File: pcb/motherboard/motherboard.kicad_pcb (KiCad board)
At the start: 2 copper layers, 64 parts, among them J1 BOOT PIN HEADER, J2 ST-Link, J3 UART_USB, J4 I2C_HEADER, SW1 STM_RST, SW2 GEN_MAZE, SW3 TOGGLE_MAZE, SW4 SOLVE_MAZE, U1 STM32F103C8Tx, U2 CH340C, U3 TPS5420D, U4 TPS5420D, U5 AMS1117-3.3, U6 PCA9306D, Y1 8MHz, Y2 32.768KHz

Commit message: placed general position of motherboard pcb components
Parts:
- added J10: M20-7820646, KiCad:HDRV6W70P0X254_1X6_1564X250X850P, F.Cu at (246.6, 51.6)
- added J11: M20-7820646, KiCad:HDRV6W70P0X254_1X6_1564X250X850P, F.Cu at (246.6, 55.7)
- added J12: M20-7820646, KiCad:HDRV6W70P0X254_1X6_1564X250X850P, F.Cu at (246.6, 59.7)
- added J13: M20-7820646, KiCad:HDRV6W70P0X254_1X6_1564X250X850P, F.Cu at (246.6, 63.8)
- added J14: M20-7820646, KiCad:HDRV6W70P0X254_1X6_1564X250X850P, F.Cu at (246.6, 67.8)
- added J15: M20-7820646, KiCad:HDRV6W70P0X254_1X6_1564X250X850P, F.Cu at (246.6, 71.9)
- added J16: M20-7820646, KiCad:HDRV6W70P0X254_1X6_1564X250X850P, F.Cu at (246.6, 75.9)
- added J5: KPJX-4S-S, KiCad1:KPJX4SS, F.Cu at (69.2, 20.5)
- added J6: SPI_TEST, Connector_PinHeader_2.54mm:PinHeader_1x05_P2.54mm_Vertical, F.Cu at (237.2, 106.7)
- added J7: M20-7820646, KiCad:HDRV6W70P0X254_1X6_1564X250X850P, F.Cu at (246.6, 39.5)
- added J8: M20-7820646, KiCad:HDRV6W70P0X254_1X6_1564X250X850P, F.Cu at (246.6, 43.5)
- added J9: M20-7820646, KiCad:HDRV6W70P0X254_1X6_1564X250X850P, F.Cu at (246.6, 47.6)
- added TP1: GND, TestPoint:TestPoint_Pad_2.0x2.0mm, F.Cu at (237.0, 90.2)
- added TP2: 3V3, TestPoint:TestPoint_Pad_2.0x2.0mm, F.Cu at (237.0, 94.3)
- added TP3: 5V, TestPoint:TestPoint_Pad_2.0x2.0mm, F.Cu at (237.0, 98.3)
- added TP4: 5V5, TestPoint:TestPoint_Pad_2.0x2.0mm, F.Cu at (237.0, 102.4)
- added TP5: UART_RX, TestPoint:TestPoint_Pad_2.0x2.0mm, F.Cu at (241.0, 90.2)
- added TP6: UART_TX, TestPoint:TestPoint_Pad_2.0x2.0mm, F.Cu at (241.0, 94.3)
- added TP7: 12V, TestPoint:TestPoint_Pad_2.0x2.0mm, F.Cu at (241.0, 98.3)
- added U7: 74HC138, Package_SO:SOIC-16_3.9x9.9mm_P1.27mm, F.Cu at (184.9, 49.3)
- moved SW1 155.7 mm to (37.6, 93.2)
- moved R2 143.4 mm to (42.2, 96.0), turned to 180 degrees
- moved C5 142.2 mm to (42.2, 93.2), turned to 180 degrees
- moved Y2 138.0 mm to (51.3, 99.1), turned to 90 degrees
- moved Y1 137.6 mm to (51.3, 103.6), turned to 90 degrees
- moved C10 128.8 mm to (56.4, 94.5), turned to 180 degrees
- moved C7 128.2 mm to (56.4, 93.0), turned to 180 degrees
- moved C9 127.9 mm to (56.4, 109.2)
- moved C8 117.8 mm to (66.5, 109.2)
- moved U2 116.9 mm to (51.8, 138.2)
- moved R12 116.4 mm to (69.7, 65.7)
- moved R11 116.4 mm to (69.6, 63.8)
- moved C15 116.1 mm to (42.0, 133.4)
- moved C16 115.1 mm to (74.5, 40.5)
- moved C6 113.2 mm to (71.1, 98.6)
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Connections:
- U1 pad 13: /STM32/PA4 -> /SPI_CS
- U1 pad 14: /STM32/PA5 -> /SPI_CLK
- U1 pad 15: /STM32/PA6 -> /SPI_MISO
- U1 pad 16: /STM32/PA7 -> /SPI_MOSI
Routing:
- net Net-(U3-VSNS): vias 0 -> 2
- net Net-(D2-K): vias 0 -> 2
- net Net-(D1-K): vias 0 -> 2
- net GND: vias 0 -> 19
- net /USB_D-: vias 0 -> 2
- net /USB_D+: vias 0 -> 2
- net /UART_TX: vias 0 -> 2
- net /UART_RX: vias 0 -> 2
- net /TG_MAZE: vias 0 -> 1
- net /STM32/RST: vias 0 -> 1
- net /STM32/PB7: vias 0 -> 2
- net /STM32/PB6: vias 0 -> 2
- net /STM32/PB5: vias 0 -> 2
- net /STM32/PB11: vias 0 -> 2
- net /STM32/PB10: vias 0 -> 5
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
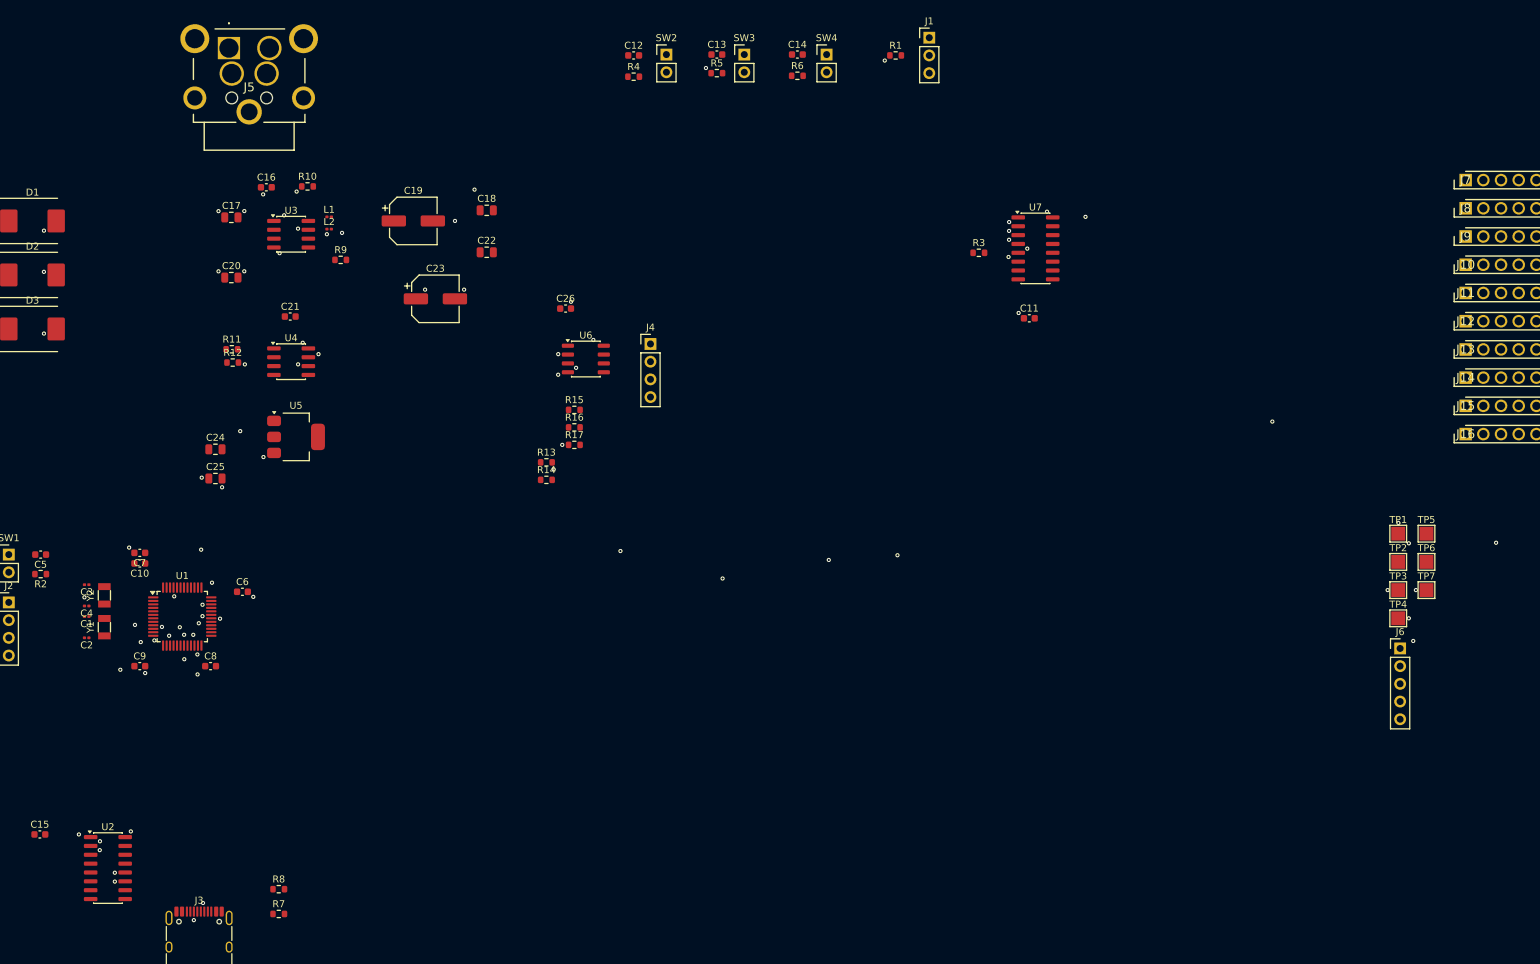
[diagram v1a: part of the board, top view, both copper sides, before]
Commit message: consolidated BOM for motherboard, added terminal blocks for external motors
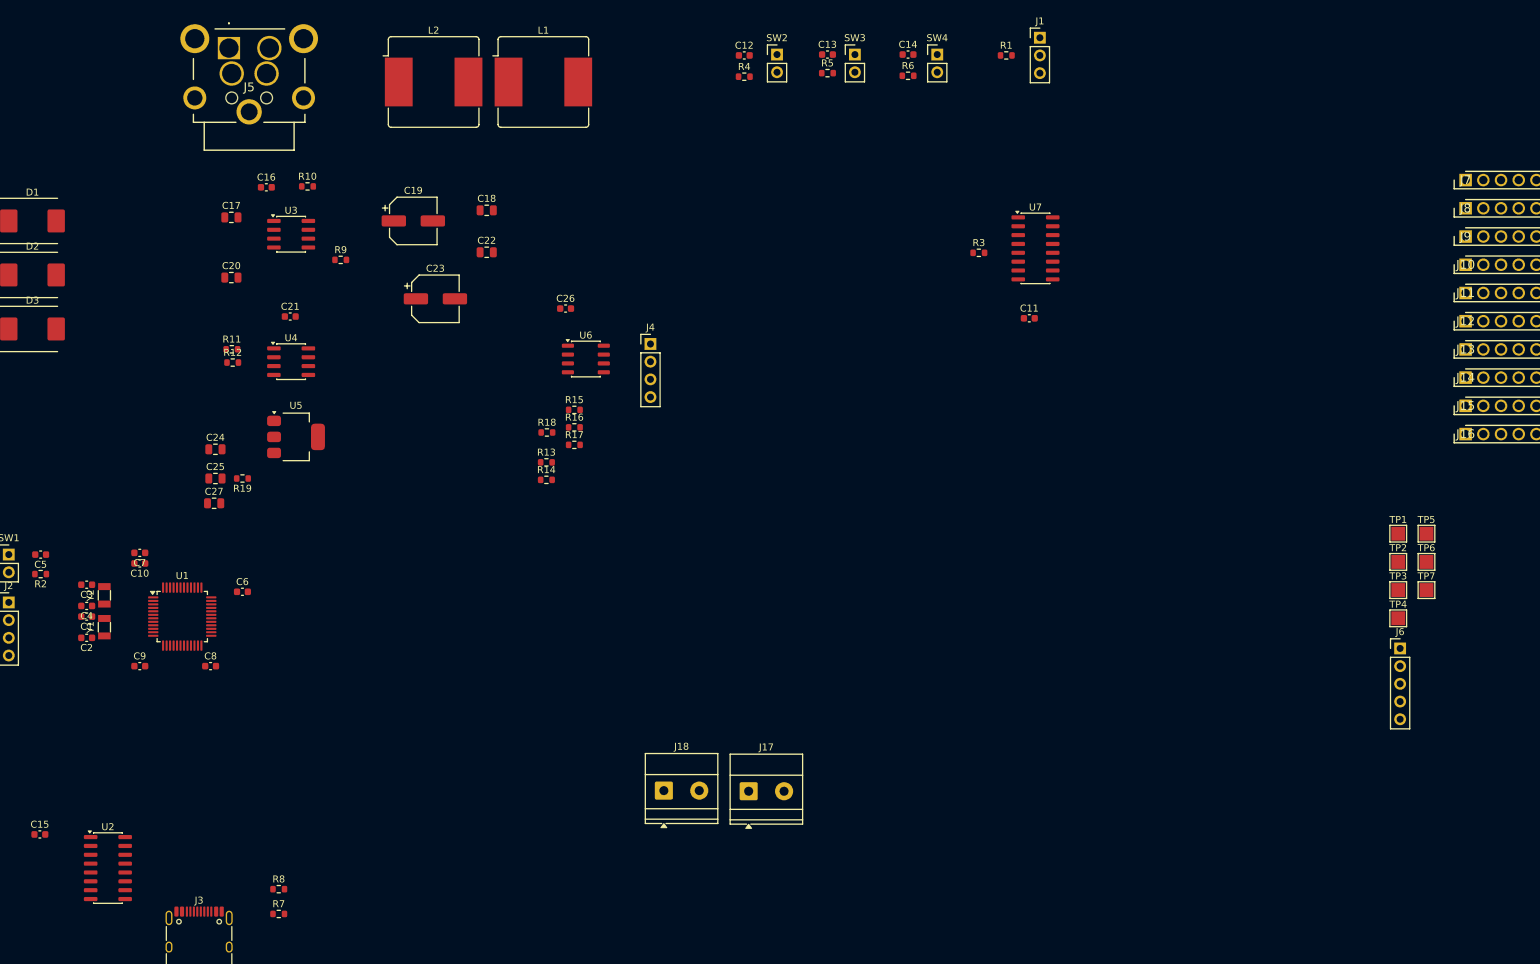
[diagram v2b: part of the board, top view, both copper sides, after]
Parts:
- added C27: 10uF, Capacitor_SMD:C_0805_2012Metric, F.Cu at (67.1, 85.9)
- added J17: Terminal 1, TerminalBlock_Phoenix:TerminalBlock_Phoenix_MKDS-1,5-2-5.08_1x02_P5.08mm_Horizontal, F.Cu at (143.8, 127.2)
- added J18: Terminal 2, TerminalBlock_Phoenix:TerminalBlock_Phoenix_MKDS-1,5-2-5.08_1x02_P5.08mm_Horizontal, F.Cu at (131.6, 127.1)
- added R18: 100k, Resistor_SMD:R_0603_1608Metric, F.Cu at (114.8, 75.7)
- added R19: 0.5, Resistor_SMD:R_0603_1608Metric, F.Cu at (71.1, 82.3)
- C1, C2, C3, C4: footprint Capacitor_SMD:C_0201_0603Metric -> Capacitor_SMD:C_0603_1608Metric
- C25: value 22uF -> 10uF
- L1, L2: footprint Inductor_SMD:L_0201_0603Metric -> Inductor_SMD:L_Bourns_SRR1208_12.7x12.7mm
- R13, R14, R15, R16: value 4.7k -> 5.1k
- R17: value 200k -> 100k
- moved L1 36.3 mm to (114.3, 25.4)
- moved L2 25.9 mm to (98.6, 25.4)
- moved C13 15.9 mm to (155.1, 21.5)
- moved C14 15.9 mm to (166.6, 21.5)
- moved J1 15.9 mm to (185.5, 19.1)
- moved R1 15.9 mm to (180.7, 21.6)
- moved R5 15.9 mm to (155.1, 24.1)
- moved R6 15.9 mm to (166.6, 24.5)
- moved SW2 15.9 mm to (147.8, 21.5)
- moved SW3 15.9 mm to (159.0, 21.5)
- moved SW4 15.9 mm to (170.8, 21.5)
- moved C12 15.9 mm to (143.1, 21.6)
- moved R4 15.9 mm to (143.1, 24.6)
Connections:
- C25 pad 2: GND -> Net-(C25-Pad2)
- R17 pad 1: +5V -> Net-(R17-Pad1)
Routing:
- net Net-(U3-VSNS): vias 2 -> 0
- net Net-(D2-K): vias 2 -> 0
- net Net-(D1-K): vias 2 -> 0
- net GND: vias 19 -> 0
- net /USB_D-: vias 2 -> 0
- net /USB_D+: vias 2 -> 0
- net /UART_TX: vias 2 -> 0
- net /UART_RX: vias 2 -> 0
- net /TG_MAZE: vias 1 -> 0
- net /STM32/RST: vias 1 -> 0
- net /STM32/PB7: vias 2 -> 0
- net /STM32/PB6: vias 2 -> 0
- net /STM32/PB5: vias 2 -> 0
- net /STM32/PB11: vias 2 -> 0
- net /STM32/PB10: vias 5 -> 0
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
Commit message: added 3d models for remaining components
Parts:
- added H1: MountingHole, MountingHole:MountingHole_4.3mm_M4, F.Cu at (162.6, 154.9)
- added H2: MountingHole, MountingHole:MountingHole_4.3mm_M4, F.Cu at (162.6, 165.1)
- added H3: MountingHole, MountingHole:MountingHole_4.3mm_M4, F.Cu at (162.6, 175.2)
- added H4: MountingHole, MountingHole:MountingHole_4.3mm_M4, F.Cu at (162.6, 185.4)
- moved J18 144.5 mm to (29.5, 24.8)
- moved J17 144.5 mm to (41.7, 24.9)
- moved J6 46.1 mm to (275.3, 132.6)
- moved TP5 46.1 mm to (279.1, 116.1)
- moved TP6 46.1 mm to (279.1, 120.2)
- moved TP7 46.1 mm to (279.1, 124.2)
- moved TP1 46.1 mm to (275.1, 116.1)
- moved TP2 46.1 mm to (275.1, 120.2)
- moved TP3 46.1 mm to (275.1, 124.2)
- moved TP4 46.1 mm to (275.1, 128.3)
- moved C11 29.7 mm to (156.1, 49.1)
- moved R3 29.7 mm to (148.8, 39.8)
- moved U7 29.7 mm to (157.0, 39.1)
- moved J16 27.5 mm to (265.9, 56.4)
- moved J10 27.5 mm to (265.9, 32.1)
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
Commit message: finished initial PCB layout for motherboard
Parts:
- removed H2: MountingHole, MountingHole:MountingHole_4.3mm_M4
- removed J10, J12, J14, J16, J8: M20-7820646, KiCad:HDRV6W70P0X254_1X6_1564X250X850P
- added C28: 220uF, Capacitor_SMD:CP_Elec_6.3x5.4, F.Cu at (180.0, 49.4)
- added C29: 220uF, Capacitor_SMD:CP_Elec_6.3x5.4, F.Cu at (149.8, 49.4)
- added C30: 220uF, Capacitor_SMD:CP_Elec_6.3x5.4, F.Cu at (157.4, 49.4)
- added C31: 220uF, Capacitor_SMD:CP_Elec_6.3x5.4, F.Cu at (164.9, 49.4)
- added C32: 220uF, Capacitor_SMD:CP_Elec_6.3x5.4, F.Cu at (172.4, 49.4)
- added J19: Terminal Block, TerminalBlock_Phoenix:TerminalBlock_Phoenix_MKDS-1,5-3-5.08_1x03_P5.08mm_Horizontal, F.Cu at (198.5, 57.0)
- added J20: Terminal Block, TerminalBlock_Phoenix:TerminalBlock_Phoenix_MKDS-1,5-3-5.08_1x03_P5.08mm_Horizontal, F.Cu at (198.5, 73.2)
- added J21: Terminal Block, TerminalBlock_Phoenix:TerminalBlock_Phoenix_MKDS-1,5-3-5.08_1x03_P5.08mm_Horizontal, F.Cu at (198.5, 89.5)
- added J22: Terminal Block, TerminalBlock_Phoenix:TerminalBlock_Phoenix_MKDS-1,5-3-5.08_1x03_P5.08mm_Horizontal, F.Cu at (198.5, 105.8)
- added J23: Terminal Block, TerminalBlock_Phoenix:TerminalBlock_Phoenix_MKDS-1,5-3-5.08_1x03_P5.08mm_Horizontal, F.Cu at (198.5, 122.0)
- added TP8: GND, TestPoint:TestPoint_Pad_2.0x2.0mm, F.Cu at (157.7, 125.6)
- moved J6 169.3 mm to (116.0, 75.3)
- moved TP4 169.1 mm to (127.7, 45.3)
- moved TP1 168.5 mm to (122.1, 45.3)
- moved TP2 167.9 mm to (122.1, 50.9)
- moved TP3 164.6 mm to (127.7, 50.9)
- moved J18 161.6 mm to (146.4, 136.3)
- moved J17 161.6 mm to (158.6, 136.4)
- moved TP5 159.8 mm to (135.8, 45.3)
- moved TP6 159.1 mm to (135.8, 50.9)
- moved J5 150.1 mm to (175.5, 126.6)
- moved D1 141.7 mm to (166.3, 111.3), turned to -90 degrees
- moved H3 137.9 mm to (111.3, 47.2)
- moved D2 126.6 mm to (150.1, 117.4)
- moved TP7 116.4 mm to (162.8, 125.6)
- moved C17 109.5 mm to (160.7, 105.5), turned to 180 degrees
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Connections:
- R3 pad 1: GND -> /daughterboard_selector/EN2
- U7 pad 6: +3V3 -> /daughterboard_selector/EN2
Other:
- board outline added: 100 x 100 mm

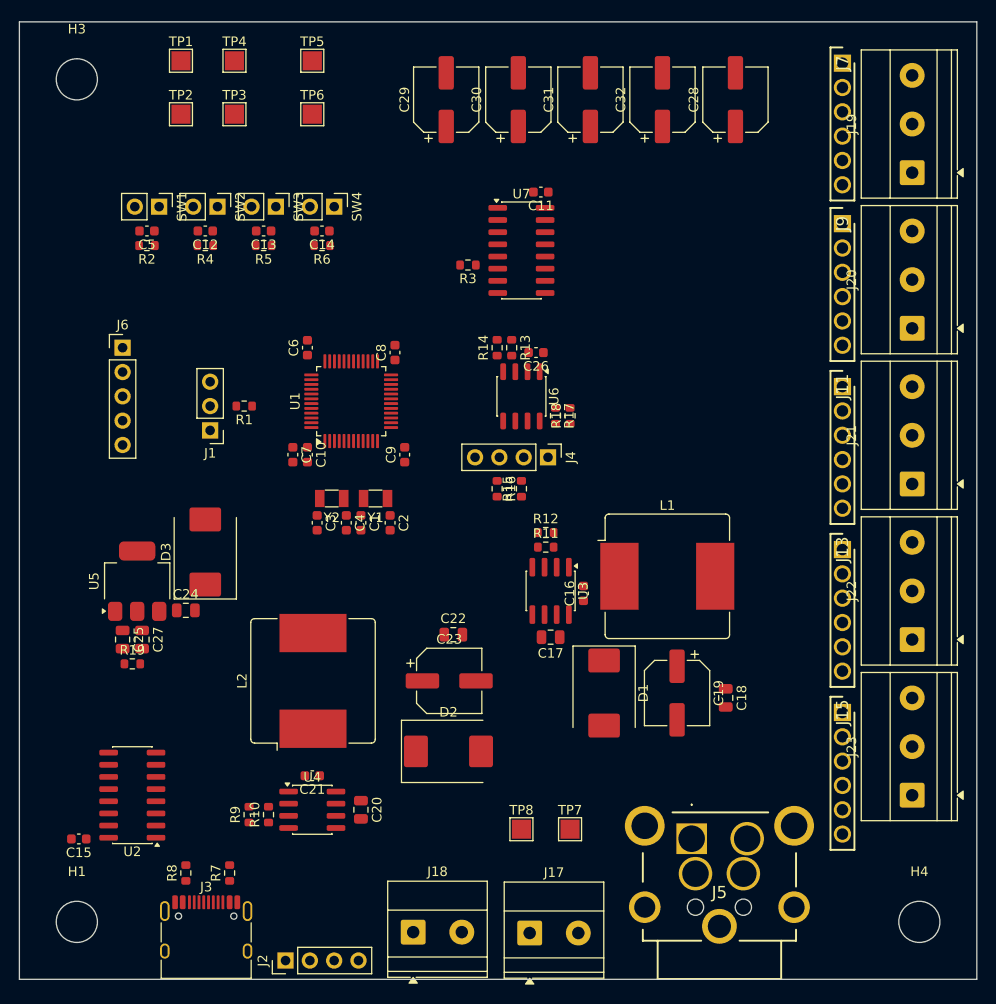
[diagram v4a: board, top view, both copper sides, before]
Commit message: added connectors for external motors, finished most of the motherboard PCB
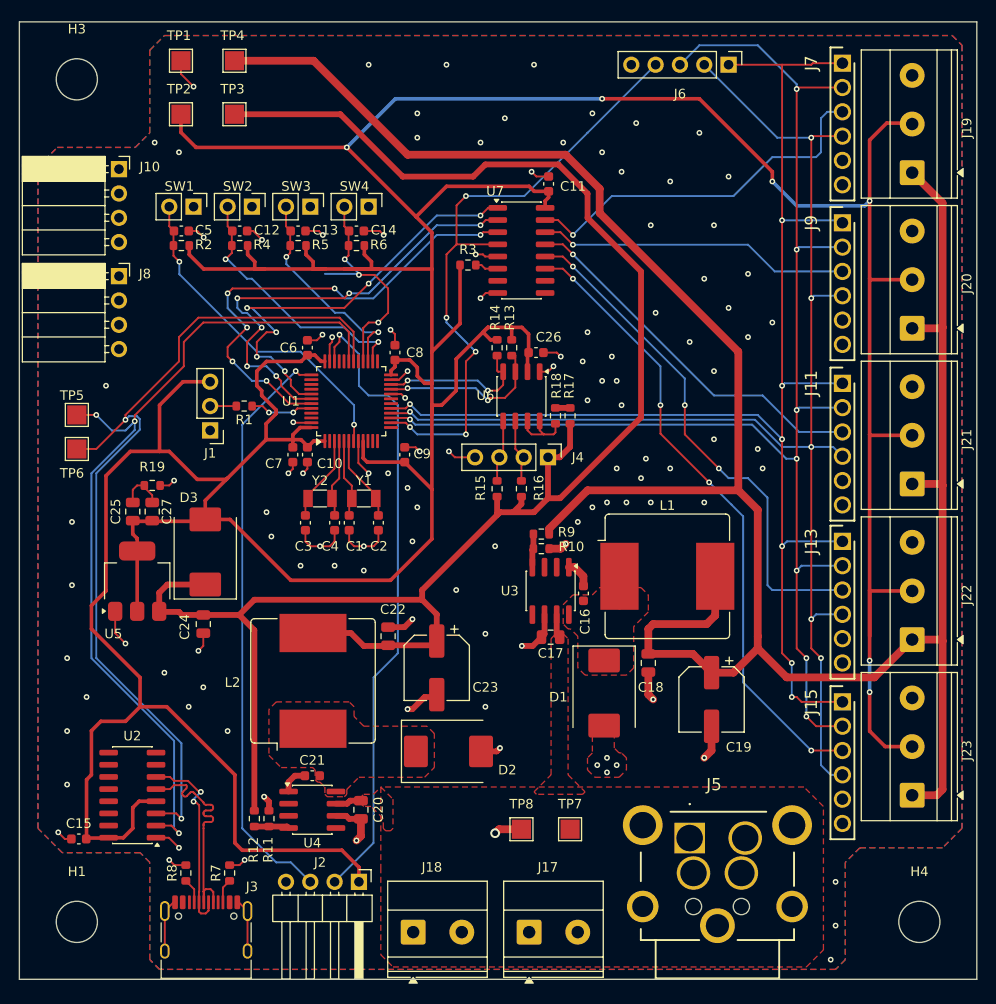
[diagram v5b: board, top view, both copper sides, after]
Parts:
- removed C28, C29, C30, C31, C32: 220uF, Capacitor_SMD:CP_Elec_6.3x5.4
- added J10: Conn_01x04, Connector_PinSocket_2.54mm:PinSocket_1x04_P2.54mm_Horizontal, F.Cu at (115.7, 56.6)
- added J8: Conn_01x04, Connector_PinSocket_2.54mm:PinSocket_1x04_P2.54mm_Horizontal, F.Cu at (115.7, 67.8)
- J2: footprint Connector_PinHeader_2.54mm:PinHeader_1x04_P2.54mm_Vertical -> Connector_PinHeader_2.54mm:PinHeader_1x04_P2.54mm_Horizontal
- moved J6 69.9 mm to (179.3, 45.7), turned to -90 degrees
- moved TP5 44.4 mm to (111.3, 82.3)
- moved TP6 42.7 mm to (111.3, 85.9)
- moved R12 42.7 mm to (129.8, 124.5), turned to 90 degrees
- moved R9 42.3 mm to (159.8, 94.7), turned to 0 degrees
- moved R11 40.5 mm to (131.3, 124.5), turned to 90 degrees
- moved R10 39.8 mm to (159.8, 96.3), turned to 0 degrees
- moved R19 18.7 mm to (119.1, 89.7), turned to 180 degrees
- moved C27 13.4 mm to (119.1, 92.4), turned to 90 degrees
- moved C25 13.4 mm to (117.1, 92.4), turned to 90 degrees
- moved J2 11.2 mm to (140.7, 131.1), turned to -90 degrees
- moved C18 8.87 mm to (170.9, 108.2)
- moved C22 6.81 mm to (143.8, 105.4), turned to 90 degrees
- moved C19 3.66 mm to (177.5, 112.0)
- moved SW1 3.60 mm to (123.4, 60.5)
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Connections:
- U1 pad 10: /GEN_MAZE -> /STM32/PA0
- U1 pad 11: /TG_MAZE -> /STM32/PA1
- U1 pad 12: /SOLVE_MAZE -> /STM32/PA2
- U1 pad 13: /SPI_CS -> /STM32/PA3
- U1 pad 14: /SPI_CLK -> /SPI_CS
- U1 pad 15: /SPI_MISO -> /SPI_CLK
- U1 pad 16: /SPI_MOSI -> /SPI_MISO
- U1 pad 17: unconnected-(U1-PA7-Pad17) -> /SPI_MOSI
- U1 pad 18: unconnected-(U1-PB0-Pad18) -> /STM32/PB0
- U1 pad 19: unconnected-(U1-PB1-Pad19) -> /STM32/PB1
- U1 pad 26: unconnected-(U1-PB13-Pad26) -> /GEN_MAZE
- U1 pad 27: unconnected-(U1-PB14-Pad27) -> /TG_MAZE
- U1 pad 28: unconnected-(U1-PB15-Pad28) -> /SOLVE_MAZE
- U1 pad 29: unconnected-(U1-PA8-Pad29) -> /STM32/PA8
- U1 pad 32: unconnected-(U1-PA11-Pad32) -> /STM32/PA11
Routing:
- net +3V3: track 0.00 -> 527.1 mm, vias 0 -> 6
- net +5V5: track 0.00 -> 245.9 mm
- net +5V: track 0.00 -> 189.2 mm
- net /SPI_CLK: track 0.00 -> 149.1 mm, vias 0 -> 8
- net /SPI_MOSI: track 0.00 -> 145.9 mm, vias 0 -> 7
- net /SPI_MISO: track 0.00 -> 142.2 mm, vias 0 -> 6
- net GND: track 0.00 -> 115.7 mm, vias 0 -> 118
- net /UART_TX: track 0.00 -> 92.0 mm, vias 0 -> 2
- net /UART_RX: track 0.00 -> 90.6 mm, vias 0 -> 3
- net /STM32/PA13: track 0.00 -> 66.6 mm, vias 0 -> 1
- net /SPI_CS4: track 0.00 -> 66.2 mm, vias 0 -> 4
- net /SPI_CS: track 0.00 -> 65.6 mm, vias 0 -> 5
- net /STM32/PA14: track 0.00 -> 61.3 mm, vias 0 -> 1
- net /SPI_CS3: track 0.00 -> 54.3 mm, vias 0 -> 3
- net /STM32/PB7: track 0.00 -> 50.8 mm, vias 0 -> 6
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- added copper zone on F.Cu, net +12V
- added copper zone on B.Cu, net GND
- added copper zone on F.Cu, net GND
- added copper zone on F.Cu, net Net-(D1-K)
- added copper zone on F.Cu, net Net-(D2-K)

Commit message: motherboard PCB finished
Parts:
- moved R10 0.25 mm to (159.8, 96.0)
- moved R9 0.25 mm to (159.8, 94.5)
- moved C26 0.09 mm to (159.2, 75.7)
- moved R13 0.09 mm to (156.7, 75.2)
- moved R14 0.09 mm to (155.1, 75.2)
- moved Y1 0.09 mm to (141.2, 90.9)
- moved Y2 0.09 mm to (136.7, 90.9)
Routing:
- net /STM32/PA0: track 0.00 -> 65.0 mm, vias 0 -> 3
- net /STM32/PB1: track 0.00 -> 61.7 mm, vias 0 -> 7
- net /STM32/PA3: track 0.00 -> 61.3 mm, vias 0 -> 7
- net /STM32/PA1: track 0.00 -> 59.0 mm, vias 0 -> 3
- net /STM32/PA2: track 0.00 -> 57.9 mm, vias 0 -> 3
- net /STM32/PB0: track 0.00 -> 45.9 mm, vias 0 -> 4
- net /STM32/PA8: track 0.00 -> 36.8 mm, vias 0 -> 2
- net /STM32/PA11: track 0.00 -> 29.4 mm, vias 0 -> 3
- net /STM32/RST: track 35.2 -> 37.6 mm
- net /TG_MAZE: track 22.7 -> 20.7 mm
- net /SOLVE_MAZE: track 24.6 -> 23.3 mm, vias 3 -> 2
- net GND: track 115.7 -> 116.7 mm, vias 118 -> 297
- net /GEN_MAZE: track 27.8 -> 26.8 mm
- net /STM32/PB5: track 46.4 -> 45.9 mm
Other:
- board text added: "BRICKTEAM 2026"
